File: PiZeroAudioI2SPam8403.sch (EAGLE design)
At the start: 46 parts, among them CON1 RPI-ZERO, J1 GROVE, J2 2X2HEADER, J3 2X1-LOCKING, J4 GROVE, J5 4X1-LOCKING, Q1 DMG2305UX, U1 TXB0104PWR, U2 LSM6DS33, U3 PCM5101A, U4 DMMT5401, U5 TXS0102, U6 PAM8403

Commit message: Fit Charger Parts
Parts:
- added C21: 4.7uF, SparkFun-Capacitors:4.7UF0603
- added C25: 22uF, SparkFun-Capacitors:22UF-0805-6.3V-20%
- added D4: BLUE, SparkFun-LED:LED-BLUE0603
- added FRAME1: FRAME-LETTER, SparkFun-Aesthetics:FRAME-LETTER
- added J10: (no value), SparkFun-Connectors:CONN_01
- added J11: AMP FCI 10103594-0001LF, SparkFun-Connectors:USB_MICRO-B_HALF_PTH
- added J8: JST, SparkFun-Connectors:CONN_02-JST-2MM-SMT
- added L1: 2.2UH3A, SparkFun-Coils:INDUCTOR-IFSC1515AHER2R2M01
- added R10: 1k, SparkFun-Resistors:1KOHM-0603-1/10W-1%
- added R11, R15: 750K, SparkFun-Resistors:750KOHM-0603-1/10W-1%
- added R12: 100k, SparkFun-Resistors:100KOHM-0603-1/10W-1%
- added R13: DNP, SparkFun-Resistors:100KOHM-0603-1/10W-1%
- added RPROG: 2.0k, SparkFun-Resistors:2.0KOHM-0603-1/10W-5%
- added TP1: TEST-POINT3, SparkFun-Connectors:TEST-POINT3
- added U7: MCP73831, SparkFun-IC-Power:MCP73831
- added U8: PAM2401, SparkFun-IC-Power:PAM2401
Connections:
- new net +5VCHARGE: C21.1, J11.VBUS, Q1.D, R10.2, U4G$2.E, U7.VIN
- new net EN: J10.1, R15.1, U8.EN
- new net N$15: RPROG.1, U7.PROG
- new net N$16: D4.C, TP1.1, U7.STAT
- new net N$17: R11.1, R12.2, U8.FB
- new net N$18: L1.2, U8.LX
- new net N$19: R13.2, U8.RSET
- new net N$23: D4.A, R10.1
- new net VBATT: C25.1, J8.1, L1.1, R15.2, U7.VBAT, U8.VIN
- net +5V: now also R11.2, U8.OUT; no longer Q1.D, U4G$2.E
- net AGND: now also C21.2, C25.2, J11.GND, J8.2, R12.1, R13.1, RPROG.2, U7.VSS, U8.AGND, U8.PGND
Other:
- note added: "2.0K resistor placed for 500mA charge rate"
- note added: "Angelo Fraietta"
- note added: "Battery connection"
- note added: "Charge power"
- note added: "Charger"
- note added: "Enable"
- note added: "Enable pin: To disable output, short EN pin to ground (is pulled up with 10kOhm)"
- note added: "For heavy duty use: Use 2A switch in switch bypass pins, or jump with wire."
- note added: "Install 100k resistor for inductor current limit"
- note added: "Ireg = 1000V/Rprog"
- note added: "LiPo Charger Booster"
- note added: "Output capacity: 5V, 1A for 3.0V to 4.2V battery voltage."
- note added: "Switch bypass"
- note added: "Switching Regulator"
- note added: "To charge battery, Minimize output load (or disable) Supply 3.75 to 6V, 500mA capable to USB or input voltage pins."

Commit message: Routed to Audio
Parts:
- removed J10: (no value), SparkFun-Connectors:CONN_01
- removed TP1: TEST-POINT3, SparkFun-Connectors:TEST-POINT3
- C21: device SparkFun-Capacitors:4.7UF0603 -> SparkFun-Capacitors:4.7UF-0603-6.3V-(10%)
- L1: value 2.2UH3A -> IFSC1515AHER2R2M01; device SparkFun-Coils:INDUCTOR-IFSC1515AHER2R2M01 -> HappyBrackets:IFSC1515AHER2R2M01
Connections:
- net N$10 renamed L-
- net N$13 renamed R-
- net N$14 renamed R+
- net N$8 renamed L+
- net +3V3: no longer JP1.1
- net AGND: now also C18.2, C19.-
- net EN: now also JP1.1; no longer J10.1
- net GND: no longer C18.2, C19.-
- net N$16: no longer TP1.1
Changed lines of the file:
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@@
 <part name="SUPPLY21" library="supply2" library_urn="urn:adsk.eagle:library:372" deviceset="GND" device=""/>
 <part name="SUPPLY17" library="supply2" library_urn="urn:adsk.eagle:library:372" deviceset="GND" device=""/>
-<part name="SUPPLY18" library="supply2" library_urn="urn:adsk.eagle:library:372" deviceset="GND" device=""/>
 <part name="FRAME1" library="SparkFun-Aesthetics" deviceset="FRAME-LETTER" device=""/>
-<part name="C21" library="SparkFun-Capacitors" deviceset="4.7UF" device="0603" value="4.7uF"/>
+<part name="C21" library="SparkFun-Capacitors" deviceset="4.7UF" device="-0603-6.3V-(10%)" value="4.7uF"/>
 <part name="D4" library="SparkFun-LED" deviceset="LED-BLUE" device="0603" value="BLUE"/>
 <part name="R10" library="SparkFun-Resistors" deviceset="1KOHM" device="-0603-1/10W-1%" value="1k"/>
@@
 <part name="J8" library="SparkFun-Connectors" deviceset="CONN_02" device="-JST-2MM-SMT" value="JST"/>
 <part name="C25" library="SparkFun-Capacitors" deviceset="22UF" device="-0805-6.3V-20%" value="22uF"/>
-<part name="J10" library="SparkFun-Connectors" deviceset="CONN_01" device=""/>
 <part name="J11" library="SparkFun-Connectors" deviceset="USB_MICRO-B" device="_HALF_PTH" value="AMP FCI 10103594-0001LF"/>
-<part name="TP1" library="SparkFun-Connectors" deviceset="TEST-POINT" device="3"/>
 <part name="R15" library="SparkFun-Resistors" deviceset="750KOHM" device="-0603-1/10W-1%" value="750K"/>
-<part name="L1" library="SparkFun-Coils" deviceset="INDUCTOR" device="-IFSC1515AHER2R2M01" value="2.2UH3A"/>
+<part name="L1" library="HappyBrackets" library_urn="urn:adsk.eagle:library:5224691" deviceset="IFSC1515AHER2R2M01" device="" value="IFSC1515AHER2R2M01"/>
 <part name="AGND11" library="supply1" library_urn="urn:adsk.eagle:library:371" deviceset="AGND" device=""/>
 <part name="AGND13" library="supply1" library_urn="urn:adsk.eagle:library:371" deviceset="AGND" device=""/>
@@
 <part name="AGND20" library="supply1" library_urn="urn:adsk.eagle:library:371" deviceset="AGND" device=""/>
 <part name="P+5" library="supply1" library_urn="urn:adsk.eagle:library:371" deviceset="+5V" device=""/>
+<part name="AGND21" library="supply1" library_urn="urn:adsk.eagle:library:371" deviceset="AGND" device=""/>
 </parts>
 <sheets>
@@
 <text x="-345.44" y="83.82" size="1.778" layer="91">To Speakers</text>
 <text x="-10.16" y="170.18" size="3.302" layer="97" font="vector">Charger</text>
-<text x="-91.44" y="88.9" size="3.302" layer="97" font="vector">Switching Regulator</text>
+<text x="-73.66" y="99.06" size="3.302" layer="97" font="vector">Switching Regulator</text>
 <text x="22.098" y="13.97" size="2.1844" layer="94" font="vector">Angelo Fraietta</text>
 <text x="10.16" y="111.76" size="1.778" layer="97" font="vector">2.0K resistor placed for
@@
  5V, 1A for 3.0V to 4.2V
  battery voltage.</text>
-<text x="-139.7" y="73.66" size="2.54" layer="97" font="vector" align="top-left">Enable pin:
+<text x="-386.08" y="243.84" size="2.54" layer="97" font="vector" align="top-left">Enable pin:
  To disable output,
  short EN pin to
@@
 <instance part="SUPPLY21" gate="GND" x="-393.7" y="58.42" smashed="yes"/>
 <instance part="SUPPLY17" gate="GND" x="-401.32" y="101.6" smashed="yes"/>
-<instance part="SUPPLY18" gate="GND" x="-375.92" y="101.6" smashed="yes"/>
 <instance part="FRAME1" gate="V" x="2.54" y="2.54"/>
 <instance part="C21" gate="G$1" x="-22.86" y="142.24"/>
@@
 <instance part="J8" gate="G$1" x="60.96" y="149.86" rot="R180"/>
 <instance part="C25" gate="G$1" x="-88.9" y="58.42"/>
-<instance part="J10" gate="G$1" x="-99.06" y="43.18"/>
 <instance part="J11" gate="G$1" x="-55.88" y="144.78" smashed="yes" rot="MR0">
 <attribute name="VALUE" x="-78.74" y="134.874" size="1.778" layer="96" font="vector" rot="MR180" align="top-left"/>
 <attribute name="NAME" x="-53.34" y="152.4" size="1.778" layer="95" font="vector" rot="MR0"/>
 </instance>
-<instance part="TP1" gate="G$1" x="-10.16" y="162.56"/>
 <instance part="R15" gate="G$1" x="-78.74" y="50.8" rot="R90"/>
-<instance part="L1" gate="G$1" x="-63.5" y="66.04" rot="R90"/>
+<instance part="L1" gate="A" x="-55.88" y="66.04" smashed="yes" rot="R180">
+<attribute name="VALUE" x="-95.9612" y="84.6328" size="3.4798" layer="96" ratio="10" rot="SR0"/>
+<attribute name="NAME" x="-54.9656" y="62.6872" size="3.4798" layer="95" ratio="10" rot="SR180"/>
+</instance>
 <instance part="AGND11" gate="VR1" x="-22.86" y="134.62" smashed="yes"/>
 <instance part="AGND13" gate="VR1" x="12.7" y="129.54" smashed="yes"/>
@@
 <attribute name="VALUE" x="-40.64" y="86.36" size="1.778" layer="96" rot="R90"/>
 </instance>
+<instance part="AGND21" gate="VR1" x="-375.92" y="101.6"/>
 </instances>
 <busses>
@@
 <pinref part="C17" gate="G$1" pin="2"/>
 <pinref part="SUPPLY17" gate="GND" pin="GND"/>
-</segment>
-<segment>
-<pinref part="C18" gate="G$1" pin="2"/>
-<pinref part="C19" gate="G$1" pin="-"/>
-<wire x1="-386.08" y1="104.14" x2="-375.92" y2="104.14" width="0.1524" layer="91"/>
-<pinref part="SUPPLY18" gate="GND" pin="GND"/>
-<wire x1="-375.92" y1="104.14" x2="-375.412" y2="104.14" width="0.1524" layer="91"/>
-<junction x="-375.92" y="104.14"/>
 </segment>
 </net>
@@
 <wire x1="-345.44" y1="231.14" x2="-332.74" y2="231.14" width="0.1524" layer="91"/>
 <junction x="-345.44" y="231.14"/>
-<wire x1="-332.74" y1="231.14" x2="-327.66" y2="231.14" width="0.1524" layer="91"/>
-<wire x1="-327.66" y1="231.14" x2="-327.66" y2="228.6" width="0.1524" layer="91"/>
-<junction x="-332.74" y="231.14"/>
-<pinref part="JP1" gate="A" pin="1"/>
-<wire x1="-327.66" y1="228.6" x2="-317.5" y2="228.6" width="0.1524" layer="91"/>
 </segment>
 <segment>
@@
 <pinref part="AGND20" gate="VR1" pin="AGND"/>
 </segment>
+<segment>
+<pinref part="C18" gate="G$1" pin="2"/>
+<pinref part="C19" gate="G$1" pin="-"/>
+<wire x1="-386.08" y1="104.14" x2="-375.92" y2="104.14" width="0.1524" layer="91"/>
+<wire x1="-375.92" y1="104.14" x2="-375.412" y2="104.14" width="0.1524" layer="91"/>
+<pinref part="AGND21" gate="VR1" pin="AGND"/>
+<junction x="-375.92" y="104.14"/>
+</segment>
 </net>
 <net name="AUDIO-LEFT" class="0">
@@
 </segment>
 </net>
-<net name="N$8" class="0">
+<net name="L+" class="0">
 <segment>
 <pinref part="U6" gate="G$1" pin="+OUTL-1"/>
@@
 </segment>
 </net>
-<net name="N$10" class="0">
+<net name="L-" class="0">
 <segment>
 <pinref part="J5" gate="G$1" pin="3"/>
@@
 </segment>
 </net>
-<net name="N$13" class="0">
+<net name="R-" class="0">
 <segment>
 <pinref part="J5" gate="G$1" pin="2"/>
@@
 </segment>
 </net>
-<net name="N$14" class="0">
+<net name="R+" class="0">
 <segment>
 <pinref part="J5" gate="G$1" pin="1"/>
@@
 </segment>
 <segment>
-<wire x1="-68.58" y1="66.04" x2="-78.74" y2="66.04" width="0.1524" layer="91"/>
+<wire x1="-71.12" y1="66.04" x2="-78.74" y2="66.04" width="0.1524" layer="91"/>
 <wire x1="-78.74" y1="58.42" x2="-76.2" y2="58.42" width="0.1524" layer="91"/>
 <junction x="-78.74" y="66.04"/>
@@
 <wire x1="-78.74" y1="55.88" x2="-78.74" y2="58.42" width="0.1524" layer="91"/>
 <junction x="-78.74" y="58.42"/>
-<pinref part="L1" gate="G$1" pin="1"/>
+<pinref part="L1" gate="A" pin="1"/>
 <junction x="-88.9" y="66.04"/>
 <wire x1="-88.9" y1="66.04" x2="-88.9" y2="68.58" width="0.1524" layer="91"/>
@@
 <pinref part="D4" gate="G$1" pin="C"/>
 <wire x1="-15.24" y1="157.48" x2="-12.7" y2="157.48" width="0.1524" layer="91"/>
-<pinref part="TP1" gate="G$1" pin="1"/>
-<wire x1="-10.16" y1="162.56" x2="-12.7" y2="162.56" width="0.1524" layer="91"/>
-<wire x1="-12.7" y1="162.56" x2="-12.7" y2="157.48" width="0.1524" layer="91"/>
-<junction x="-12.7" y="157.48"/>
 </segment>
 </net>
@@
 <label x="-86.36" y="43.18" size="1.778" layer="95" font="vector" rot="MR0"/>
 <pinref part="U8" gate="G$1" pin="EN"/>
-<pinref part="J10" gate="G$1" pin="1"/>
 <pinref part="R15" gate="G$1" pin="1"/>
 <wire x1="-78.74" y1="43.18" x2="-76.2" y2="43.18" width="0.1524" layer="91"/>
 <wire x1="-78.74" y1="45.72" x2="-78.74" y2="43.18" width="0.1524" layer="91"/>
 <junction x="-78.74" y="43.18"/>
+<label x="-91.44" y="43.18" size="1.778" layer="95" rot="R180" xref="yes"/>
+</segment>
+<segment>
+<pinref part="JP1" gate="A" pin="1"/>
+<wire x1="-327.66" y1="231.14" x2="-327.66" y2="228.6" width="0.1524" layer="91"/>
+<wire x1="-327.66" y1="228.6" x2="-317.5" y2="228.6" width="0.1524" layer="91"/>
+<label x="-330.2" y="236.22" size="1.778" layer="95" rot="R180" xref="yes"/>
+<wire x1="-330.2" y1="236.22" x2="-327.66" y2="236.22" width="0.1524" layer="91"/>
+<wire x1="-327.66" y1="236.22" x2="-327.66" y2="231.14" width="0.1524" layer="91"/>
 </segment>
 </net>
@@
 <net name="N$18" class="0">
 <segment>
-<wire x1="-58.42" y1="66.04" x2="-48.26" y2="66.04" width="0.1524" layer="91"/>
+<wire x1="-55.88" y1="66.04" x2="-48.26" y2="66.04" width="0.1524" layer="91"/>
 <wire x1="-48.26" y1="66.04" x2="-48.26" y2="58.42" width="0.1524" layer="91"/>
 <wire x1="-48.26" y1="58.42" x2="-50.8" y2="58.42" width="0.1524" layer="91"/>
 <pinref part="U8" gate="G$1" pin="LX"/>
-<pinref part="L1" gate="G$1" pin="2"/>
-</segment>
-</net>
+<pinref part="L1" gate="A" pin="2"/>
+</segment>
+</net>

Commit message: Routed with ratsnest
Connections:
- net R+: now also J5.2; no longer J5.1
- net R-: now also J5.1; no longer J5.2
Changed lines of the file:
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@@
 <net name="R-" class="0">
 <segment>
-<pinref part="J5" gate="G$1" pin="2"/>
-<wire x1="-360.934" y1="82.296" x2="-365.76" y2="82.296" width="0.1524" layer="91"/>
 <pinref part="U6" gate="G$1" pin="-OUT_R-14"/>
-<wire x1="-365.76" y1="82.296" x2="-365.76" y2="78.74" width="0.1524" layer="91"/>
 <wire x1="-365.76" y1="78.74" x2="-370.84" y2="78.74" width="0.1524" layer="91"/>
+<wire x1="-365.76" y1="78.74" x2="-360.68" y2="78.74" width="0.1524" layer="91"/>
+<pinref part="J5" gate="G$1" pin="1"/>
+<wire x1="-360.68" y1="78.74" x2="-360.68" y2="79.756" width="0.1524" layer="91"/>
+<wire x1="-360.68" y1="79.756" x2="-360.934" y2="79.756" width="0.1524" layer="91"/>
 </segment>
 </net>
 <net name="R+" class="0">
 <segment>
-<pinref part="J5" gate="G$1" pin="1"/>
 <pinref part="U6" gate="G$1" pin="+OUT_R-16"/>
-<wire x1="-360.934" y1="79.756" x2="-360.934" y2="73.66" width="0.1524" layer="91"/>
-<wire x1="-360.934" y1="73.66" x2="-370.84" y2="73.66" width="0.1524" layer="91"/>
+<pinref part="J5" gate="G$1" pin="2"/>
+<wire x1="-363.22" y1="73.66" x2="-370.84" y2="73.66" width="0.1524" layer="91"/>
+<wire x1="-360.934" y1="82.296" x2="-363.22" y2="82.296" width="0.1524" layer="91"/>
+<wire x1="-363.22" y1="82.296" x2="-363.22" y2="73.66" width="0.1524" layer="91"/>
 </segment>
 </net>

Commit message: Changed Footprints for consistency
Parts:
- removed C25: 22uF, SparkFun-Capacitors:22UF-0805-6.3V-20%
- removed FRAME1: FRAME-LETTER, SparkFun-Aesthetics:FRAME-LETTER
- removed J11: AMP FCI 10103594-0001LF, SparkFun-Connectors:USB_MICRO-B_HALF_PTH
- removed J8: JST, SparkFun-Connectors:CONN_02-JST-2MM-SMT
- removed RPROG: 2.0k, SparkFun-Resistors:2.0KOHM-0603-1/10W-5%
- added C22: 22uF, resistor:C-EUC0603
- added J6: GROVE, HappyBrackets:GROVE
- added J7: 4X1-LOCKING, HappyBrackets:4X1-LOCKING
- added R14: 100k, adafruit:R-US_R0603
- C13: value 10uF -> 4.7uF; device HappyBrackets:CAP-POLARISED1206-POLAR -> SparkFun-Capacitors:4.7UF-0603-6.3V-(10%)
- C14: value 0.1uF -> 10uF; device rcl:C-EUC0603 -> HappyBrackets:CAP-POLARISED1206-POLAR
- C15: value 10uF -> 0.1uF; device HappyBrackets:CAP-POLARISED1206-POLAR -> rcl:C-EUC0603
- C16: value 1uF -> 10uF; device rcl:C-EUC0603 -> HappyBrackets:CAP-POLARISED1206-POLAR
- C19: value 470uF -> 1uF; device HappyBrackets:CAP-POLARISED2917-POLAR -> rcl:C-EUC0603
- C20: value 0.1uF -> 470uF; device rcl:C-EUC0603 -> HappyBrackets:CAP-POLARISED2917-POLAR
- C21: value 4.7uF -> 0.1uF; device SparkFun-Capacitors:4.7UF-0603-6.3V-(10%) -> rcl:C-EUC0603
- J3: value 2X1-LOCKING -> JST; device HappyBrackets:2X1-LOCKING -> SparkFun-Connectors:CONN_02-JST-2MM-SMT
- J4: value GROVE -> AMP FCI 10103594-0001LF; device HappyBrackets:GROVE -> HappyBrackets:AMP10103594-0001LF
- J5: value 4X1-LOCKING -> 2X1-LOCKING; device HappyBrackets:4X1-LOCKING -> HappyBrackets:2X1-LOCKING
- R10: value 1k -> 10K; device SparkFun-Resistors:1KOHM-0603-1/10W-1% -> adafruit:R-US_R0603
- R11: value 750K -> 10K; device SparkFun-Resistors:750KOHM-0603-1/10W-1% -> adafruit:R-US_R0603
- R12: value 100k -> 750K; device SparkFun-Resistors:100KOHM-0603-1/10W-1% -> adafruit:R-US_R0603
- R13: value DNP -> 750K; device SparkFun-Resistors:100KOHM-0603-1/10W-1% -> adafruit:R-US_R0603
- R15: value 750K -> DNP; device SparkFun-Resistors:750KOHM-0603-1/10W-1% -> adafruit:R-US_R0603
- R7: value 47K -> 1k
- R8: value 10K -> 2.0k
- R9: value 10K -> 47K
- U4: value DMMT5401 -> MCP73831; device HappyBrackets:DMMT5401 -> SparkFun-IC-Power:MCP73831
- U5: value TXS0102 -> DMMT5401; device adafruit:TXS0102 -> HappyBrackets:DMMT5401
- U6: value PAM8403 -> TXS0102; device HappyBrackets:PAM8403 -> adafruit:TXS0102
- U7: value MCP73831 -> PAM8403; device SparkFun-IC-Power:MCP73831 -> HappyBrackets:PAM8403
- renumbered D4 to D1
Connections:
- net +3V3: now also C15.2, C16.+, U6.OE, U6.VCCA; no longer C14.2, C15.+, U5.OE, U5.VCCA
- net +5V: now also C17.1, J6.3, R12.2, U6.VCCB, U7.VDD-6; no longer C16.1, J4.3, R11.2, U5.VCCB, U6.VDD-6
- net +5V-IN: now also J5.1, U5G$1.E; no longer J3.1, U4G$1.E
- net +5VCHARGE: now also C13.1, J4.VBUS, R7.2, U4.VIN, U5G$2.E; no longer C21.1, J11.VBUS, R10.2, U4G$2.E, U7.VIN
- net /MUTE: now also R11.1; no longer R9.1
- net AGND: now also C13.2, C14.-, C17.2, C19.2, C20.-, C22.2, J4.GND, J5.2, R10.2, R14.1, R15.1, R9.2, U4.VSS, U7.11-GND, U7.9-NC; no longer C13.-, C16.2, C18.2, C19.-, C20.2, C25.2, J11.GND, J8.2, R12.1, R13.1, R7.2, RPROG.2, U6.11-GND, U6.9-NC, U7.VSS
- net AN3V3: now also C14.+, C19.1, C20.+, U7.PVDD-13, U7.PVDD-4; no longer C13.+, C17.1, C19.+, U6.PVDD-13, U6.PVDD-4
- net AUDIO-LEFT: now also U7.7-INL; no longer U6.7-INL
- net AUDIO-RIGHT: now also U7.10-INR; no longer U6.10-INR
- net EN: now also R13.1; no longer R15.1
- net GND: now also C15.1, C16.-, C18.2, J6.4, U6.GND, U7.15-PGND, U7.2-PGND; no longer C14.1, C15.-, C17.2, J4.4, U5.GND, U6.15-PGND, U6.2-PGND
- net L+: now also J7.4, U7.+OUTL-1; no longer J5.4, U6.+OUTL-1
- net L-: now also J7.3, U7.-OUTL-3; no longer J5.3, U6.-OUTL-3
- net N$15: now also R8.1, U4.PROG; no longer RPROG.1, U7.PROG
- net N$16: now also U4.STAT; no longer U7.STAT
- net N$17: now also R12.1, R14.2; no longer R11.1, R12.2
- net N$19: now also R15.2; no longer R13.2
- net N$22: now also R10.1, U5G$1.B, U5G$2.B, U5G$2.C; no longer R8.1, U4G$1.B, U4G$2.B, U4G$2.C
- net N$23: now also R7.1; no longer R10.1
- net N$27: now also R9.1, U5G$1.C; no longer R7.1, U4G$1.C
- net N$5: now also R11.2, U7.12-/SHND, U7.5-/MUTE; no longer R9.2, U6.12-/SHND, U6.5-/MUTE
- net N$7: now also C21.1, U7.8-VREF; no longer C20.1, U6.8-VREF
- net R+: now also J7.2, U7.+OUT_R-16; no longer J5.2, U6.+OUT_R-16
- net R-: now also J7.1, U7.-OUT_R-14; no longer J5.1, U6.-OUT_R-14
- net SCL: now also U6.A2; no longer U5.A2
- net SCL-OUT: now also J6.1, U6.B2; no longer J4.1, U5.B2
- net SDA: now also U6.A1; no longer U5.A1
- net SDA-OUT: now also J6.2, U6.B1; no longer J4.2, U5.B1
- net VBATT: now also C22.1, J3.1, R13.2, U4.VBAT; no longer C25.1, J8.1, R15.2, U7.VBAT
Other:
- moved on the sheet: C17, C18, C21, R10, R11, R12, R13, R15, R7, R8, R9

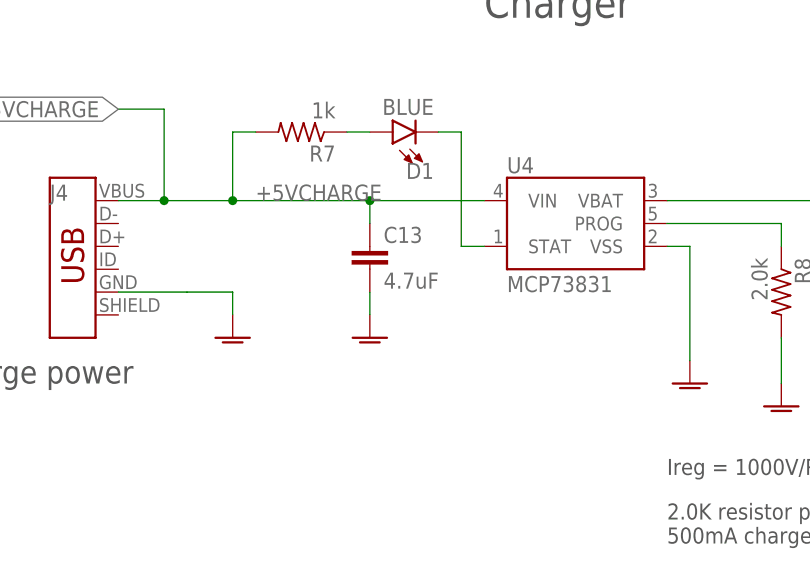
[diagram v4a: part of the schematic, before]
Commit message: Updated Capacitor footprint
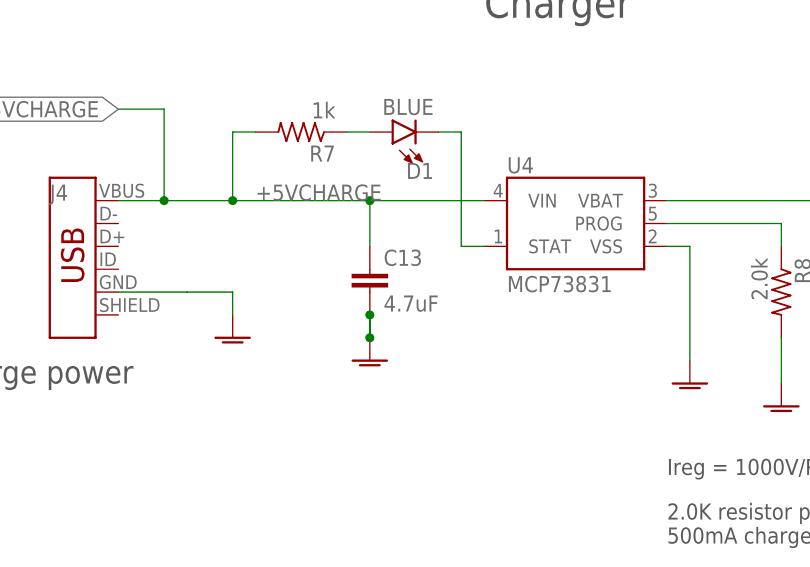
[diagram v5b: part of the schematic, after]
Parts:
- C13: device SparkFun-Capacitors:4.7UF-0603-6.3V-(10%) -> rcl:C-EUC0603
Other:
- moved on the sheet: C13
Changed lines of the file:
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@@
 <part name="SUPPLY20" library="supply2" library_urn="urn:adsk.eagle:library:372" deviceset="GND" device=""/>
 <part name="SUPPLY17" library="supply2" library_urn="urn:adsk.eagle:library:372" deviceset="GND" device=""/>
-<part name="C13" library="SparkFun-Capacitors" deviceset="4.7UF" device="-0603-6.3V-(10%)" value="4.7uF"/>
+<part name="C13" library="rcl" library_urn="urn:adsk.eagle:library:334" deviceset="C-EU" device="C0603" package3d_urn="urn:adsk.eagle:package:23616/2" value="4.7uF"/>
 <part name="D1" library="SparkFun-LED" deviceset="LED-BLUE" device="0603" value="BLUE"/>
 <part name="R7" library="adafruit" deviceset="R-US_" device="R0603" value="1k"/>
@@
 <attribute name="NAME" x="-54.9656" y="62.6872" size="3.4798" layer="95" ratio="10" rot="SR180"/>
 </instance>
-<instance part="AGND8" gate="VR1" x="-22.86" y="134.62" smashed="yes"/>
+<instance part="AGND8" gate="VR1" x="-22.86" y="132.08" smashed="yes"/>
 <instance part="AGND9" gate="VR1" x="12.7" y="129.54" smashed="yes"/>
 <instance part="AGND10" gate="VR1" x="22.86" y="127" smashed="yes"/>
@@
 </segment>
 <segment>
-<wire x1="-22.86" y1="139.7" x2="-22.86" y2="137.16" width="0.1524" layer="91"/>
 <pinref part="C13" gate="G$1" pin="2"/>
 <pinref part="AGND8" gate="VR1" pin="AGND"/>
+<wire x1="-22.86" y1="134.62" x2="-22.86" y2="137.16" width="0.1524" layer="91"/>
+<wire x1="-22.86" y1="137.16" x2="-22.86" y2="134.62" width="0.1524" layer="91"/>
+<junction x="-22.86" y="137.16"/>
+<junction x="-22.86" y="134.62"/>
 </segment>
 <segment>
@@
 <segment>
 <wire x1="-22.86" y1="149.86" x2="-10.16" y2="149.86" width="0.1524" layer="91"/>
-<wire x1="-22.86" y1="147.32" x2="-22.86" y2="149.86" width="0.1524" layer="91"/>
+<wire x1="-22.86" y1="144.78" x2="-22.86" y2="149.86" width="0.1524" layer="91"/>
 <wire x1="-38.1" y1="149.86" x2="-22.86" y2="149.86" width="0.1524" layer="91"/>
 <wire x1="-38.1" y1="157.48" x2="-38.1" y2="149.86" width="0.1524" layer="91"/>

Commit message: Changed Current Resistor to 100K
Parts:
- R15: value DNP -> 100K
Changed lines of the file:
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@@
 <part name="R12" library="adafruit" deviceset="R-US_" device="R0603" value="750K"/>
 <part name="R14" library="adafruit" deviceset="R-US_" device="R0603" value="100k"/>
-<part name="R15" library="adafruit" deviceset="R-US_" device="R0603" value="DNP"/>
+<part name="R15" library="adafruit" deviceset="R-US_" device="R0603" value="100K"/>
 <part name="U8" library="SparkFun-IC-Power" deviceset="PAM2401" device="" value="PAM2401"/>
 <part name="J3" library="SparkFun-Connectors" deviceset="CONN_02" device="-JST-2MM-SMT" value="JST"/>
